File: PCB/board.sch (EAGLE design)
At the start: 32 parts, among them IC1 MEGA1284P-SQUARE, IC2 MC33269D-3.3, J1 DCJ0202, Q1 CRYSTAL_16MHZ_SMD, Q2 BUZ10, U1 OPA564AIDWD

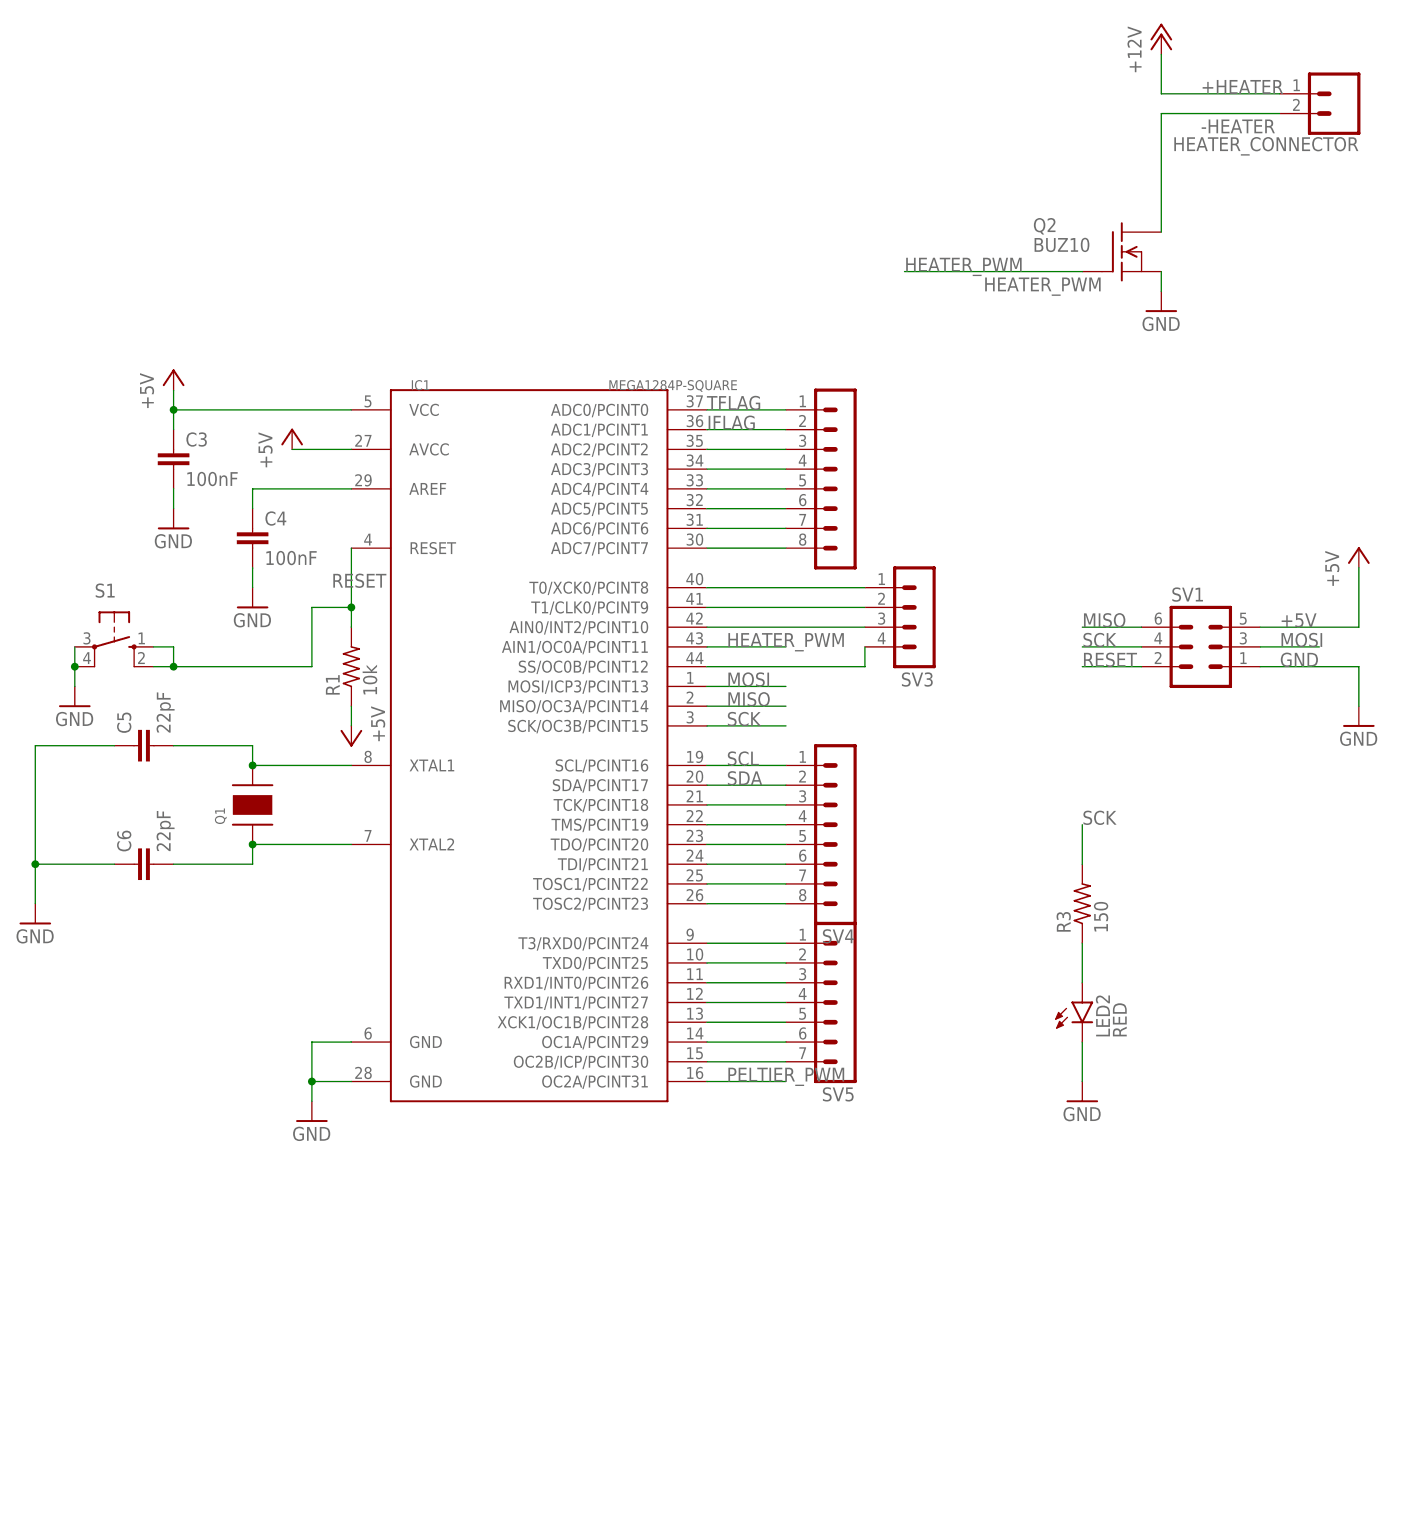
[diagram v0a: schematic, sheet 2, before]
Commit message: finished routing PCB with added pins; need silkscreen!
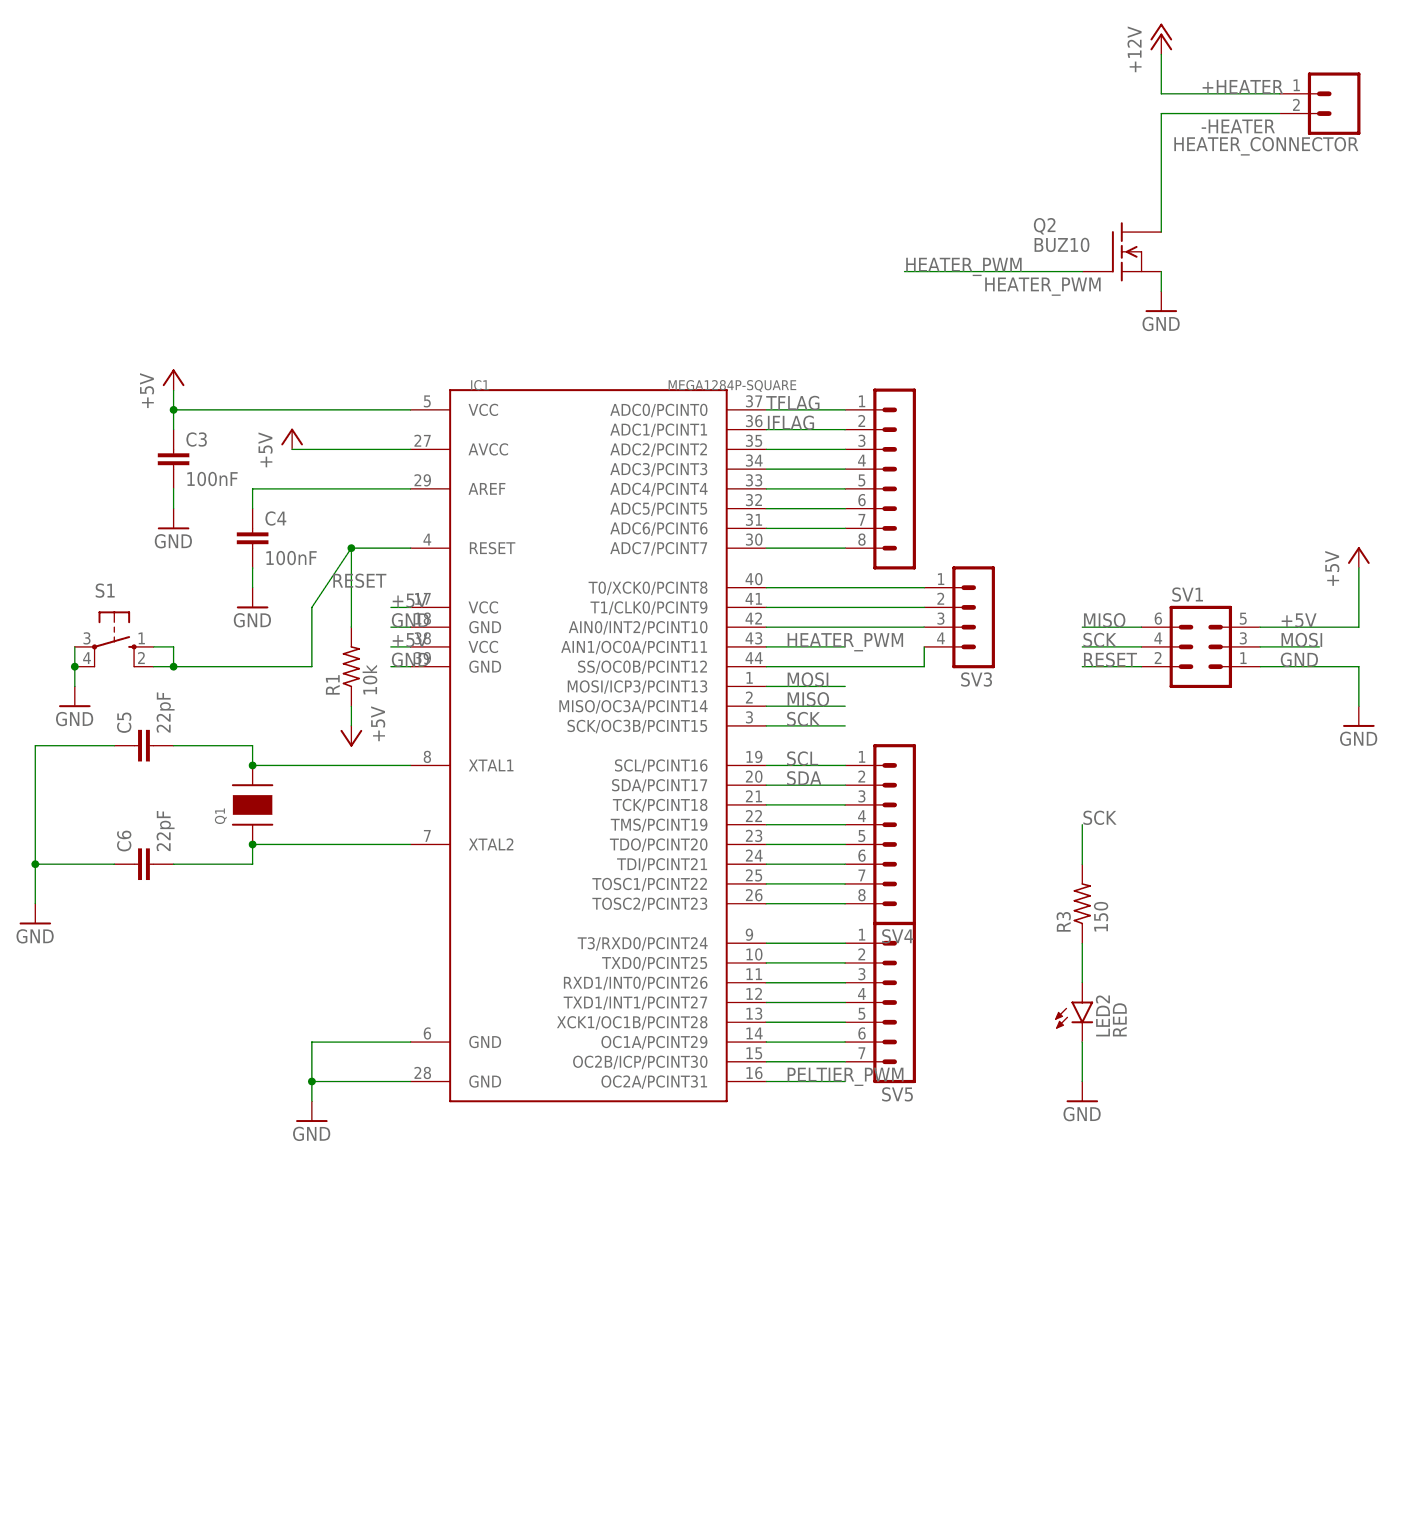
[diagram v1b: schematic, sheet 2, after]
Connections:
- net +5V: now also IC1.VCC@1, IC1.VCC@2
- net GND: now also IC1.GND@2, IC1.GND@3
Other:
- moved on the sheet: SV3, SV4, SV5

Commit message: Michael and Matthew, Silkscreening done
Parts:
- SCK_LED: value RED -> BLUE
- renumbered LED1 to 5V_LED, LED2 to SCK_LED, LED3 to 3V3_LED
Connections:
- net N$10 renamed 13
- net N$11 renamed 12
- net N$12 renamed 11
- net N$13 renamed 10
- net N$14 renamed 9
- net N$15 renamed 26
- net N$16 renamed 25
- net N$17 renamed 24
- net N$18 renamed 23
- net N$19 renamed 22
- net N$20 renamed 21
- net N$25 renamed 35
- net N$26 renamed 34
- net N$27 renamed 33
- net N$28 renamed 32
- net N$29 renamed 31
- net N$30 renamed 30
- net N$31 renamed 40
- net N$32 renamed 41
- net N$33 renamed 42
- net N$35 renamed 44
- net N$8 renamed 15
- net N$9 renamed 14

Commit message: Finalized Board #1
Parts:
- added JP1: (no value), pinhead:PINHD-1X2
- added PIN_15_LED: BLUE, led:LEDCHIP-LED0603
- added R7: 150, rcl:R-US_R0603
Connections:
- removed net +HEATER: HEATER_CONNECTOR.1
- new net N$1: PIN_15_LED.A, R7.1
- net +12V: now also HEATER_CONNECTOR.1
- net +3V3: now also JP1.1
- net 15: now also R7.2
- net GND: now also JP1.2, PIN_15_LED.C
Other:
- moved on the sheet: HEATER_CONNECTOR
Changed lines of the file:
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@@
 <?xml version="1.0" encoding="utf-8"?>
 <!DOCTYPE eagle SYSTEM "eagle.dtd">
-<eagle version="8.1.1">
+<eagle version="9.4.2">
 <drawing>
 <settings>
-<setting alwaysvectorfont="yes"/>
+<setting alwaysvectorfont="no"/>
+<setting keepoldvectorfont="yes"/>
 <setting verticaltext="up"/>
 </settings>
@@
 <part name="SV5" library="con-lstb" deviceset="MA07-1" device=""/>
 <part name="SV3" library="con-lstb" deviceset="MA04-1" device=""/>
+<part name="JP1" library="pinhead" library_urn="urn:adsk.eagle:library:325" deviceset="PINHD-1X2" device="" package3d_urn="urn:adsk.eagle:package:22435/2"/>
+<part name="GND16" library="supply1" deviceset="GND" device=""/>
+<part name="R7" library="rcl" deviceset="R-US_" device="R0603" value="150"/>
+<part name="PIN_15_LED" library="led" deviceset="LED" device="CHIP-LED0603" value="BLUE"/>
 </parts>
 <sheets>
@@
 <instance part="P+10" gate="1" x="30.48" y="30.48" smashed="yes">
 <attribute name="VALUE" x="27.94" y="25.4" size="1.778" layer="96" rot="R90"/>
+</instance>
+<instance part="JP1" gate="G$1" x="226.06" y="71.12" smashed="yes">
+<attribute name="NAME" x="219.71" y="76.835" size="1.778" layer="95"/>
+<attribute name="VALUE" x="219.71" y="66.04" size="1.778" layer="96"/>
 </instance>
 </instances>
@@
 <wire x1="149.86" y1="58.42" x2="172.72" y2="58.42" width="0.1524" layer="91"/>
 <pinref part="C8" gate="G$1" pin="2"/>
+<pinref part="JP1" gate="G$1" pin="2"/>
+<wire x1="172.72" y1="55.88" x2="223.52" y2="55.88" width="0.1524" layer="91"/>
+<wire x1="223.52" y1="55.88" x2="223.52" y2="71.12" width="0.1524" layer="91"/>
+<junction x="172.72" y="55.88"/>
 </segment>
 <segment>
@@
 <pinref part="+3V7" gate="G$1" pin="+3V3"/>
 <wire x1="200.66" y1="78.74" x2="213.36" y2="78.74" width="0.1524" layer="91"/>
-<wire x1="213.36" y1="78.74" x2="213.36" y2="86.36" width="0.1524" layer="91"/>
+<wire x1="213.36" y1="78.74" x2="213.36" y2="81.28" width="0.1524" layer="91"/>
+<wire x1="213.36" y1="81.28" x2="213.36" y2="86.36" width="0.1524" layer="91"/>
 <wire x1="200.66" y1="71.12" x2="200.66" y2="78.74" width="0.1524" layer="91"/>
 <pinref part="IC2" gate="G$1" pin="VO"/>
@@
 <junction x="200.66" y="78.74"/>
 <pinref part="C8" gate="G$1" pin="1"/>
+<pinref part="JP1" gate="G$1" pin="1"/>
+<wire x1="213.36" y1="81.28" x2="223.52" y2="81.28" width="0.1524" layer="91"/>
+<wire x1="223.52" y1="81.28" x2="223.52" y2="73.66" width="0.1524" layer="91"/>
+<junction x="213.36" y="81.28"/>
 </segment>
 <segment>
@@
 <attribute name="VALUE" x="203.2" y="149.86" size="1.778" layer="96" rot="R90"/>
 </instance>
-<instance part="HEATER_CONNECTOR" gate="G$1" x="228.6" y="147.32" smashed="yes" rot="R180">
-<attribute name="VALUE" x="231.14" y="152.146" size="1.778" layer="96" font="vector" rot="R180"/>
-<attribute name="NAME" x="231.14" y="141.732" size="1.778" layer="95" font="vector" rot="R180"/>
+<instance part="HEATER_CONNECTOR" gate="G$1" x="226.06" y="147.32" smashed="yes" rot="R180">
+<attribute name="VALUE" x="228.6" y="152.146" size="1.778" layer="96" font="vector" rot="R180"/>
+<attribute name="NAME" x="228.6" y="141.732" size="1.778" layer="95" font="vector" rot="R180"/>
 </instance>
 <instance part="SV2" gate="1" x="172.72" y="99.06" smashed="yes" rot="R180">
@@
 <attribute name="VALUE" x="184.15" y="88.9" size="1.778" layer="96" rot="R180"/>
 <attribute name="NAME" x="184.15" y="72.898" size="1.778" layer="95" rot="R180"/>
+</instance>
+<instance part="GND16" gate="1" x="182.88" y="-33.02" smashed="yes">
+<attribute name="VALUE" x="180.34" y="-35.56" size="1.778" layer="96"/>
+</instance>
+<instance part="R7" gate="G$1" x="182.88" y="-7.62" smashed="yes" rot="R90">
+<attribute name="NAME" x="181.3814" y="-11.43" size="1.778" layer="95" rot="R90"/>
+<attribute name="VALUE" x="186.182" y="-11.43" size="1.778" layer="96" rot="R90"/>
+</instance>
+<instance part="PIN_15_LED" gate="G$1" x="182.88" y="-20.32" smashed="yes">
+<attribute name="NAME" x="186.436" y="-27.432" size="1.778" layer="95" rot="R90"/>
 </instance>
 </instances>
@@
 <wire x1="109.22" y1="73.66" x2="106.68" y2="73.66" width="0.1524" layer="91"/>
 <label x="106.68" y="73.66" size="1.778" layer="95"/>
+</segment>
+<segment>
+<pinref part="PIN_15_LED" gate="G$1" pin="C"/>
+<pinref part="GND16" gate="1" pin="GND"/>
+<wire x1="182.88" y1="-25.4" x2="182.88" y2="-30.48" width="0.1524" layer="91"/>
 </segment>
 </net>
@@
 <pinref part="SV5" gate="1" pin="7"/>
 </segment>
+<segment>
+<pinref part="R7" gate="G$1" pin="2"/>
+<wire x1="182.88" y1="-2.54" x2="182.88" y2="5.08" width="0.1524" layer="91"/>
+<label x="182.88" y="5.08" size="1.778" layer="95"/>
+</segment>
 </net>
 <net name="14" class="0">
@@
 <pinref part="Q2" gate="G$1" pin="D"/>
 <wire x1="205.74" y1="129.54" x2="205.74" y2="144.78" width="0.1524" layer="91"/>
-<wire x1="205.74" y1="144.78" x2="220.98" y2="144.78" width="0.1524" layer="91"/>
+<wire x1="205.74" y1="144.78" x2="218.44" y2="144.78" width="0.1524" layer="91"/>
 <label x="210.82" y="142.24" size="1.778" layer="95"/>
 <pinref part="HEATER_CONNECTOR" gate="G$1" pin="2"/>
 </segment>
 </net>
-<net name="+HEATER" class="0">
+<net name="+12V" class="0">
 <segment>
 <wire x1="205.74" y1="147.32" x2="205.74" y2="152.4" width="0.1524" layer="91"/>
 <pinref part="P+8" gate="1" pin="+12V"/>
-<label x="210.82" y="147.32" size="1.778" layer="95"/>
-<wire x1="205.74" y1="147.32" x2="220.98" y2="147.32" width="0.1524" layer="91"/>
+<label x="210.82" y="152.4" size="1.778" layer="95"/>
+<wire x1="205.74" y1="147.32" x2="218.44" y2="147.32" width="0.1524" layer="91"/>
 <pinref part="HEATER_CONNECTOR" gate="G$1" pin="1"/>
+</segment>
+</net>
+<net name="N$1" class="0">
+<segment>
+<pinref part="R7" gate="G$1" pin="1"/>
+<pinref part="PIN_15_LED" gate="G$1" pin="A"/>
+<wire x1="182.88" y1="-12.7" x2="182.88" y2="-17.78" width="0.1524" layer="91"/>
 </segment>
 </net>
@@
 </schematic>
 </drawing>
+<compatibility>
+<note version="8.2" severity="warning">
+Since Version 8.2, EAGLE supports online libraries. The ids
+of those online libraries will not be understood (or retained)
+with this version.
+</note>
+<note version="8.3" severity="warning">
+Since Version 8.3, EAGLE supports URNs for individual library
+assets (packages, symbols, and devices). The URNs of those assets
+will not be understood (or retained) with this version.
+</note>
+<note version="8.3" severity="warning">
+Since Version 8.3, EAGLE supports the association of 3D packages
+with devices in libraries, schematics, and board files. Those 3D
+packages will not be understood (or retained) with this version.
+</note>
+</compatibility>
 </eagle>
